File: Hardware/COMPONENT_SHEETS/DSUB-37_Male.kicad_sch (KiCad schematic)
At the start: 2 parts, among them J3 D37S13A4GX00LF

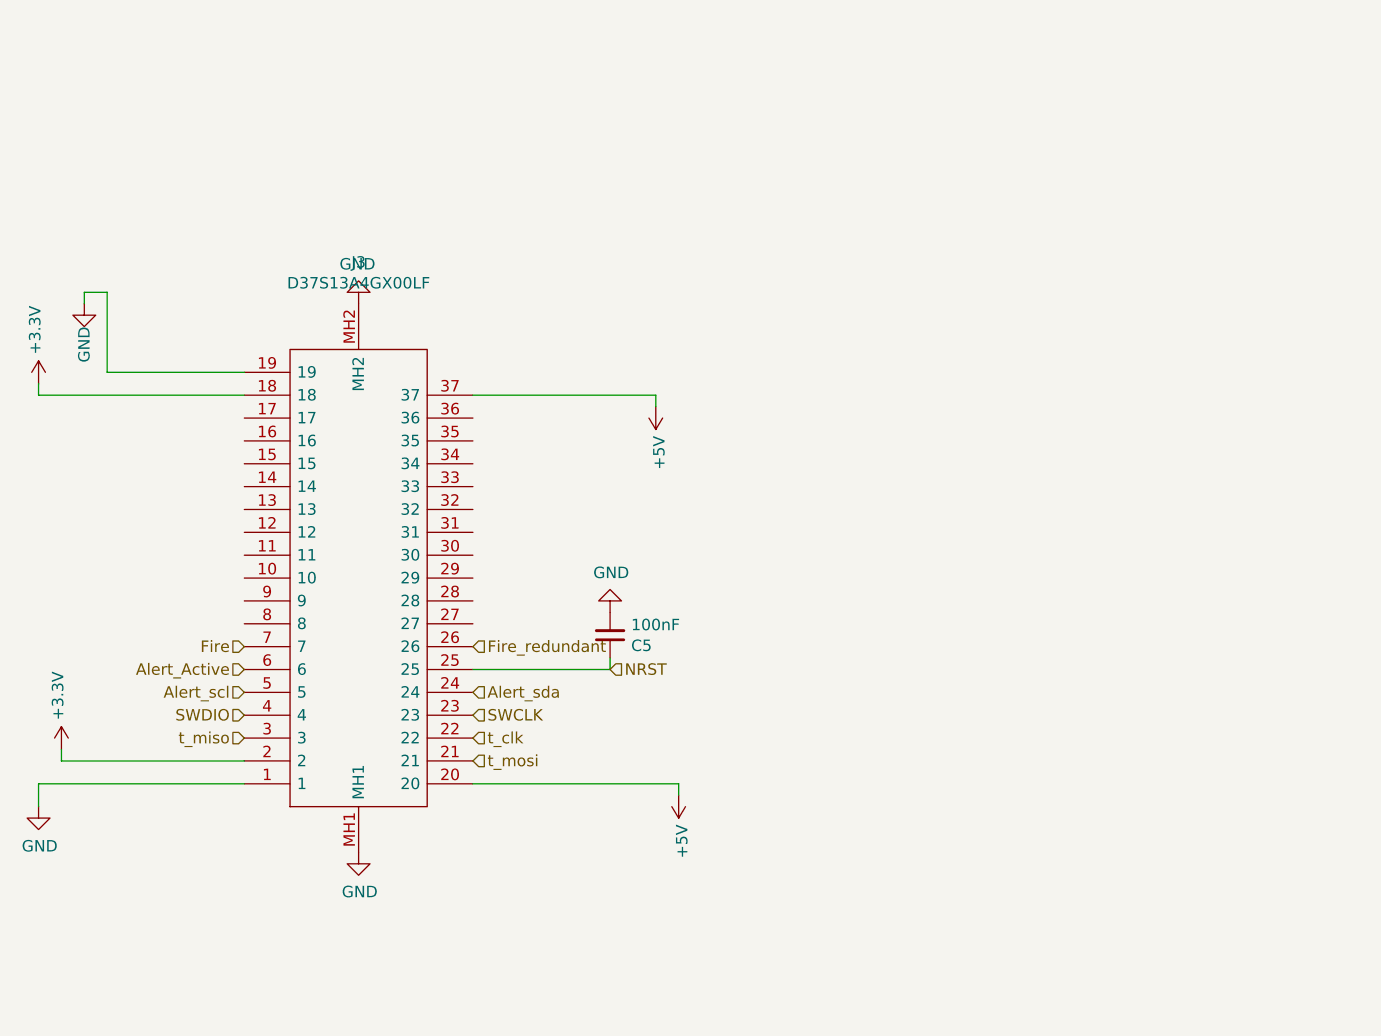
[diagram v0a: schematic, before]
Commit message: Added correct crystal for mcu, re-routing of data lines in progress
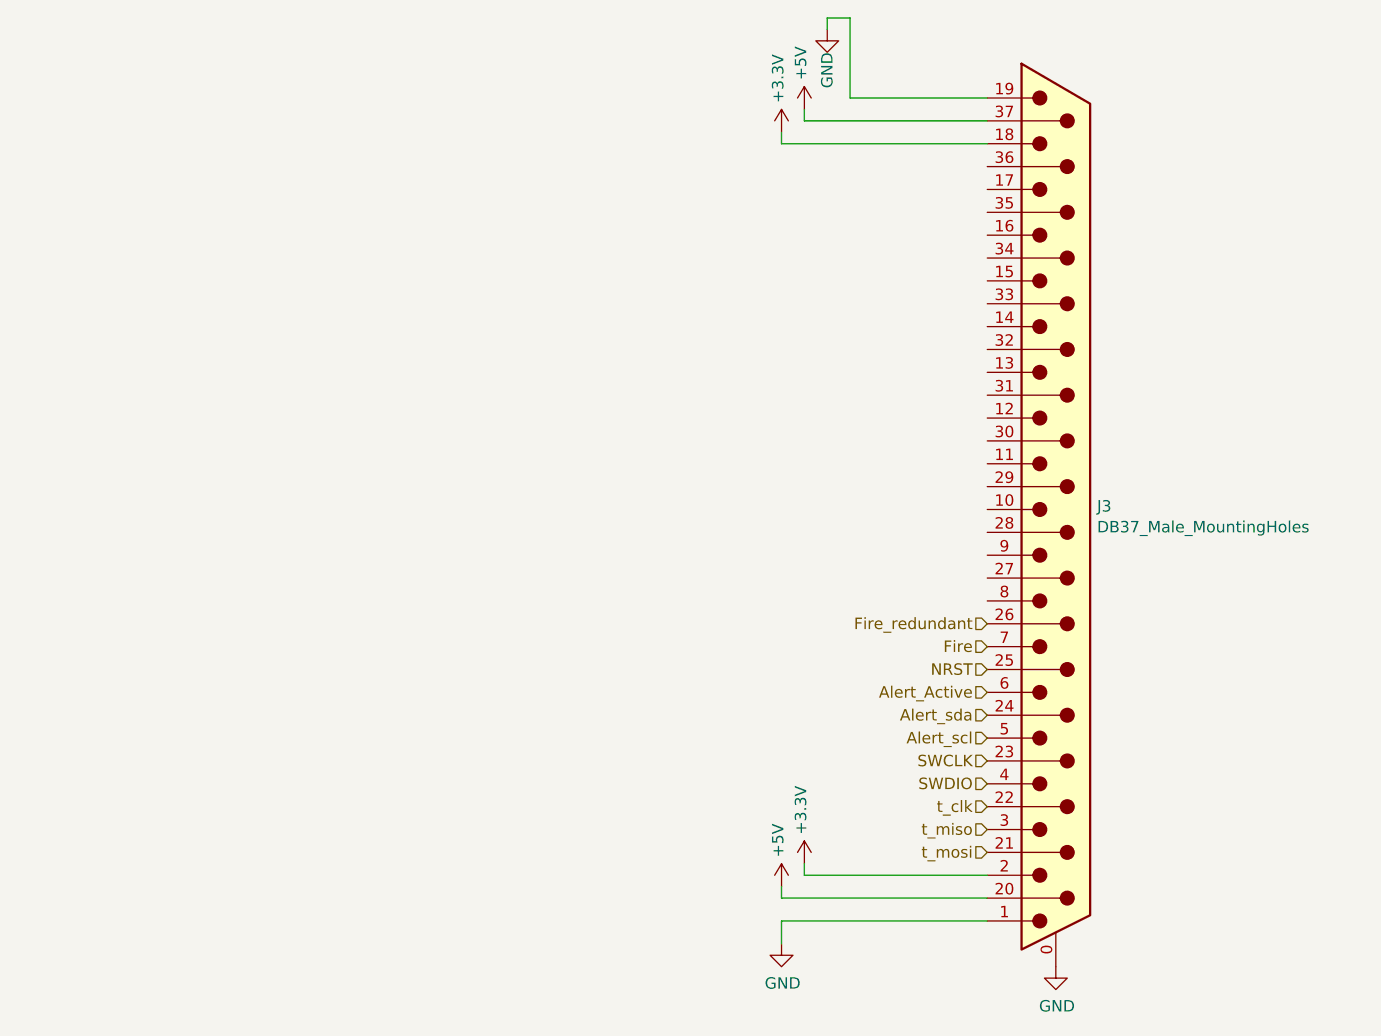
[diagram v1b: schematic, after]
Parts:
- removed C5: 100nF, Capacitor_SMD:C_0603_1608Metric, symbol Device:C_Small
- removed J3: D37S13A4GX00LF, SamacSys_Parts:D37S13A4GX00LF, symbol SamacSys_Parts:D37S13A4GX00LF
- added J3: DB37_Male_MountingHoles, RDT_Custom_Footprints:L717SDC37P1ACH4F, symbol Connector:DB37_Male_MountingHoles
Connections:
- net +3V3: now also J3.18, J3.2
- net +5V: now also J3.20, J3.37
- net Alert_Active: now also J3.6
- net Alert_scl: now also J3.5
- net Alert_sda: now also J3.24
- net Fire: now also J3.7
- net Fire_redundant: now also J3.26
- net GND: now also J3.0 (PAD), J3.1, J3.19
- net NRST: now also J3.25
- net SWCLK: now also J3.23
- net SWDIO: now also J3.4
- net t_clk: now also J3.22
- net t_miso: now also J3.3
- net t_mosi: now also J3.21

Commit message: Routed all traces and components, need to place LEDs
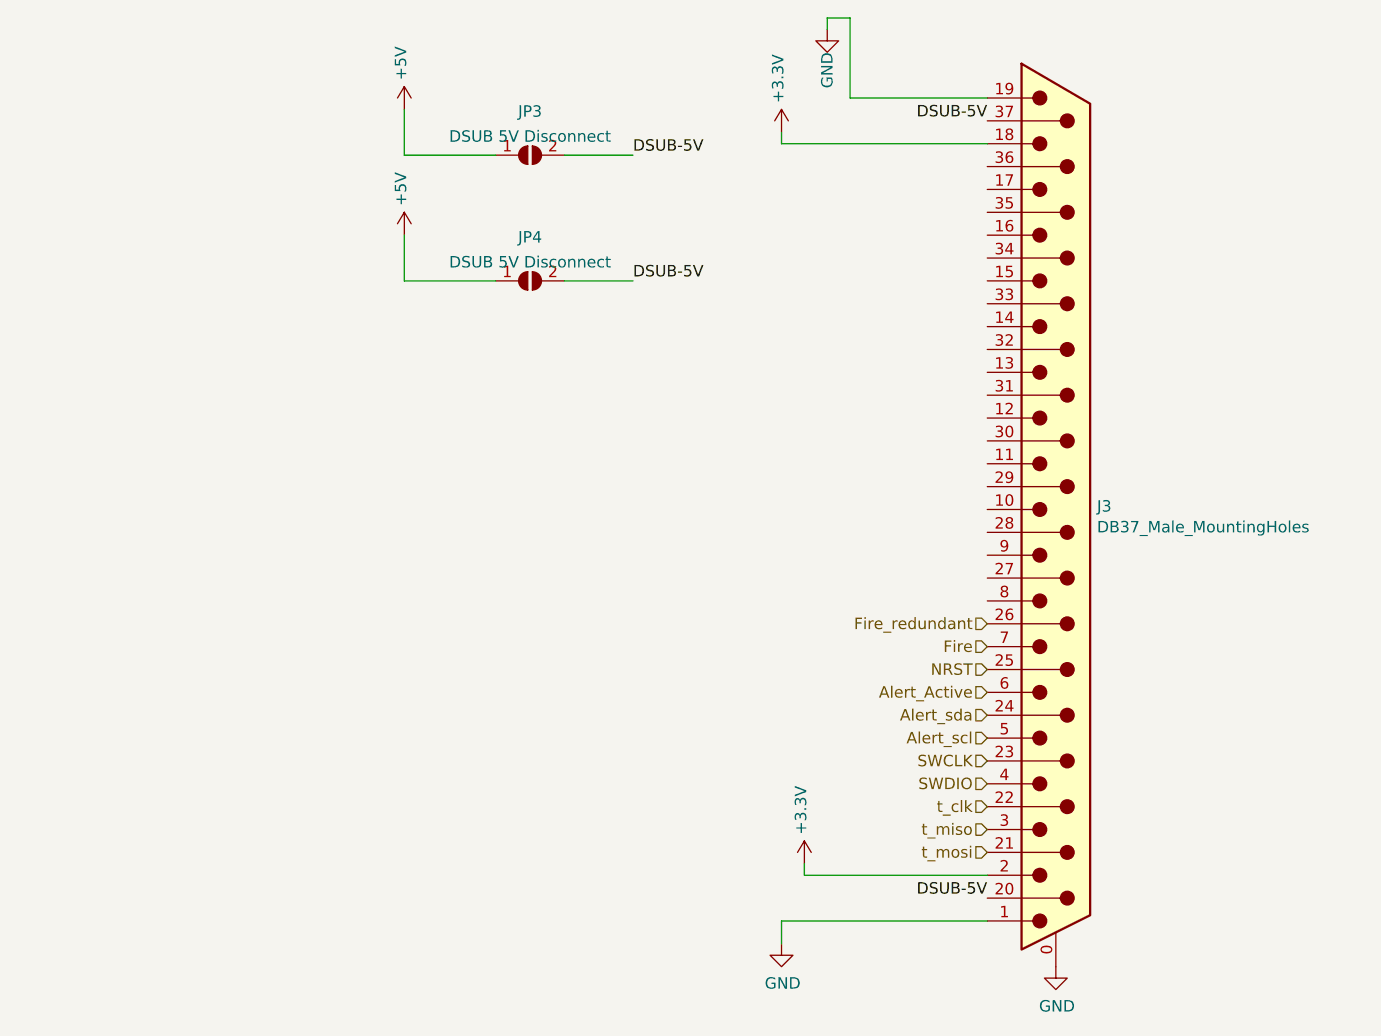
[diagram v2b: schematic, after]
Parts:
- added JP3, JP4: DSUB 5V Disconnect, Jumpers:SMT-JUMPER_2_NO_SILK, symbol Jumper:SolderJumper_2_Open
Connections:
- net +5V: now also JP3.1 (A), JP4.1 (A); no longer J3.20, J3.37
- new net DSUB-5V: J3.20, J3.37, JP3.2 (B), JP4.2 (B)
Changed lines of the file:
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@@
 (kicad_sch (version 20211123) (generator eeschema)
   (paper "A4")
-  (wire (pts (xy 189.23 120.65) (xy 189.23 119.38))
-    (stroke (width 0) (type default) (color 0 0 0 0))
-  )
   (wire (pts (xy 194.31 22.86) (xy 194.31 24.13))
     (stroke (width 0) (type default) (color 0 0 0 0))
   )
-  (wire (pts (xy 189.23 120.65) (xy 212.09 120.65))
-    (stroke (width 0) (type default) (color 0 0 0 0))
-  )
-  (wire (pts (xy 191.77 34.29) (xy 212.09 34.29))
+  (wire (pts (xy 147.32 52.07) (xy 157.48 52.07))
     (stroke (width 0) (type default) (color 0 0 0 0))
   )
@@
     (stroke (width 0) (type default) (color 0 0 0 0))
   )
-  (wire (pts (xy 191.77 34.29) (xy 191.77 33.02))
-    (stroke (width 0) (type default) (color 0 0 0 0))
-  )
   (wire (pts (xy 191.77 118.11) (xy 212.09 118.11))
     (stroke (width 0) (type default) (color 0 0 0 0))
   )
+  (wire (pts (xy 165.1 38.1) (xy 172.72 38.1))
+    (stroke (width 0) (type default) (color 0 0 0 0))
+  )
   (wire (pts (xy 189.23 123.19) (xy 212.09 123.19))
     (stroke (width 0) (type default) (color 0 0 0 0))
@@
     (stroke (width 0) (type default) (color 0 0 0 0))
   )
+  (wire (pts (xy 147.32 46.99) (xy 147.32 52.07))
+    (stroke (width 0) (type default) (color 0 0 0 0))
+  )
+  (wire (pts (xy 147.32 38.1) (xy 157.48 38.1))
+    (stroke (width 0) (type default) (color 0 0 0 0))
+  )
   (wire (pts (xy 196.85 22.86) (xy 194.31 22.86))
     (stroke (width 0) (type default) (color 0 0 0 0))
   )
+  (wire (pts (xy 165.1 52.07) (xy 172.72 52.07))
+    (stroke (width 0) (type default) (color 0 0 0 0))
+  )
+  (wire (pts (xy 147.32 33.02) (xy 147.32 38.1))
+    (stroke (width 0) (type default) (color 0 0 0 0))
+  )
   (wire (pts (xy 189.23 36.83) (xy 212.09 36.83))
     (stroke (width 0) (type default) (color 0 0 0 0))
   )
+  (label "DSUB-5V" (at 172.72 52.07 0)
+    (effects (font (size 1.27 1.27)) (justify left bottom))
+  )
+  (label "DSUB-5V" (at 212.09 120.65 180)
+    (effects (font (size 1.27 1.27)) (justify right bottom))
+  )
+  (label "DSUB-5V" (at 212.09 34.29 180)
+    (effects (font (size 1.27 1.27)) (justify right bottom))
+  )
+  (label "DSUB-5V" (at 172.72 38.1 0)
+    (effects (font (size 1.27 1.27)) (justify left bottom))
+  )
   (hierarchical_label "Alert_Active" (shape input) (at 212.09 97.79 180)
     (effects (font (size 1.27 1.27)) (justify right))
@@
   (hierarchical_label "t_clk" (shape input) (at 212.09 110.49 180)
     (effects (font (size 1.27 1.27)) (justify right))
-  )
-  (symbol (lib_id "power:+5V") (at 189.23 119.38 0) (mirror y) (unit 1)
-    (in_bom yes) (on_board yes)
-    (property "Reference" "#PWR027" (id 0) (at 189.23 123.19 0)
-      (effects (font (size 1.27 1.27)) hide)
-    )
-    (property "Value" "+5V" (id 1) (at 188.849 116.1288 90)
-      (effects (font (size 1.27 1.27)) (justify left))
-    )
-    (property "Footprint" "" (id 2) (at 189.23 119.38 0)
-      (effects (font (size 1.27 1.27)) hide)
-    )
-    (property "Datasheet" "" (id 3) (at 189.23 119.38 0)
-      (effects (font (size 1.27 1.27)) hide)
-    )
-    (pin "1")
   )
   (symbol (lib_id "power:+3.3V") (at 191.77 116.84 0) (mirror y) (unit 1)
@@
     (pin "9")
   )
-  (symbol (lib_id "power:+5V") (at 191.77 33.02 0) (mirror y) (unit 1)
-    (in_bom yes) (on_board yes)
-    (property "Reference" "#PWR029" (id 0) (at 191.77 36.83 0)
-      (effects (font (size 1.27 1.27)) hide)
-    )
-    (property "Value" "+5V" (id 1) (at 191.389 29.7688 90)
-      (effects (font (size 1.27 1.27)) (justify left))
-    )
-    (property "Footprint" "" (id 2) (at 191.77 33.02 0)
-      (effects (font (size 1.27 1.27)) hide)
-    )
-    (property "Datasheet" "" (id 3) (at 191.77 33.02 0)
+  (symbol (lib_id "power:+5V") (at 147.32 33.02 0) (mirror y) (unit 1)
+    (in_bom yes) (on_board yes)
+    (property "Reference" "#PWR029" (id 0) (at 147.32 36.83 0)
+      (effects (font (size 1.27 1.27)) hide)
+    )
+    (property "Value" "+5V" (id 1) (at 146.939 29.7688 90)
+      (effects (font (size 1.27 1.27)) (justify left))
+    )
+    (property "Footprint" "" (id 2) (at 147.32 33.02 0)
+      (effects (font (size 1.27 1.27)) hide)
+    )
+    (property "Datasheet" "" (id 3) (at 147.32 33.02 0)
       (effects (font (size 1.27 1.27)) hide)
     )
@@
     (pin "1")
   )
+  (symbol (lib_id "power:+5V") (at 147.32 46.99 0) (mirror y) (unit 1)
+    (in_bom yes) (on_board yes)
+    (property "Reference" "#PWR0110" (id 0) (at 147.32 50.8 0)
+      (effects (font (size 1.27 1.27)) hide)
+    )
+    (property "Value" "+5V" (id 1) (at 146.939 43.7388 90)
+      (effects (font (size 1.27 1.27)) (justify left))
+    )
+    (property "Footprint" "" (id 2) (at 147.32 46.99 0)
+      (effects (font (size 1.27 1.27)) hide)
+    )
+    (property "Datasheet" "" (id 3) (at 147.32 46.99 0)
+      (effects (font (size 1.27 1.27)) hide)
+    )
+    (pin "1")
+  )
+  (symbol (lib_id "Jumper:SolderJumper_2_Open") (at 161.29 38.1 0) (unit 1)
+    (in_bom yes) (on_board yes) (fields_autoplaced)
+    (property "Reference" "JP3" (id 0) (at 161.29 33.2445 0))
+    (property "Value" "DSUB 5V Disconnect" (id 1) (at 161.29 36.0196 0))
+    (property "Footprint" "Jumpers:SMT-JUMPER_2_NO_SILK" (id 2) (at 161.29 38.1 0)
+      (effects (font (size 1.27 1.27)) hide)
+    )
+    (property "Datasheet" "~" (id 3) (at 161.29 38.1 0)
+      (effects (font (size 1.27 1.27)) hide)
+    )
+    (pin "1")
+    (pin "2")
+  )
+  (symbol (lib_id "Jumper:SolderJumper_2_Open") (at 161.29 52.07 0) (unit 1)
+    (in_bom yes) (on_board yes) (fields_autoplaced)
+    (property "Reference" "JP4" (id 0) (at 161.29 47.2145 0))
+    (property "Value" "DSUB 5V Disconnect" (id 1) (at 161.29 49.9896 0))
+    (property "Footprint" "Jumpers:SMT-JUMPER_2_NO_SILK" (id 2) (at 161.29 52.07 0)
+      (effects (font (size 1.27 1.27)) hide)
+    )
+    (property "Datasheet" "~" (id 3) (at 161.29 52.07 0)
+      (effects (font (size 1.27 1.27)) hide)
+    )
+    (pin "1")
+    (pin "2")
+  )
 )
